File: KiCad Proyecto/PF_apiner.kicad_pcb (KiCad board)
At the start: 2 copper layers, 132 parts, among them J1 OBDII Header, J2 Conn_01x05, Q1 2N7002, Q10 2N7002, Q2 BSS314PE, Q3 BSS314PE, Q4 MMBT3904, Q5 MMBT3904, Q6 2N7002, Q7 2N7002, Q8 2N7002, Q9 BSS314PE, SW1 SW_RESET, SW2 SW_BOOT, U1 TPS54202, U10 STN2120, U11 AZ1117EH-3.3TRG1, U14 ESP32-WROOM, U2 AZ1117EH-3.3TRG1, U3 LM339, U4 MCP25612FD, U5 TH8056, U6 PESD1CAN, U7 PESD1CAN, U8 PESD1CAN, U9 LM317, Y1 16M

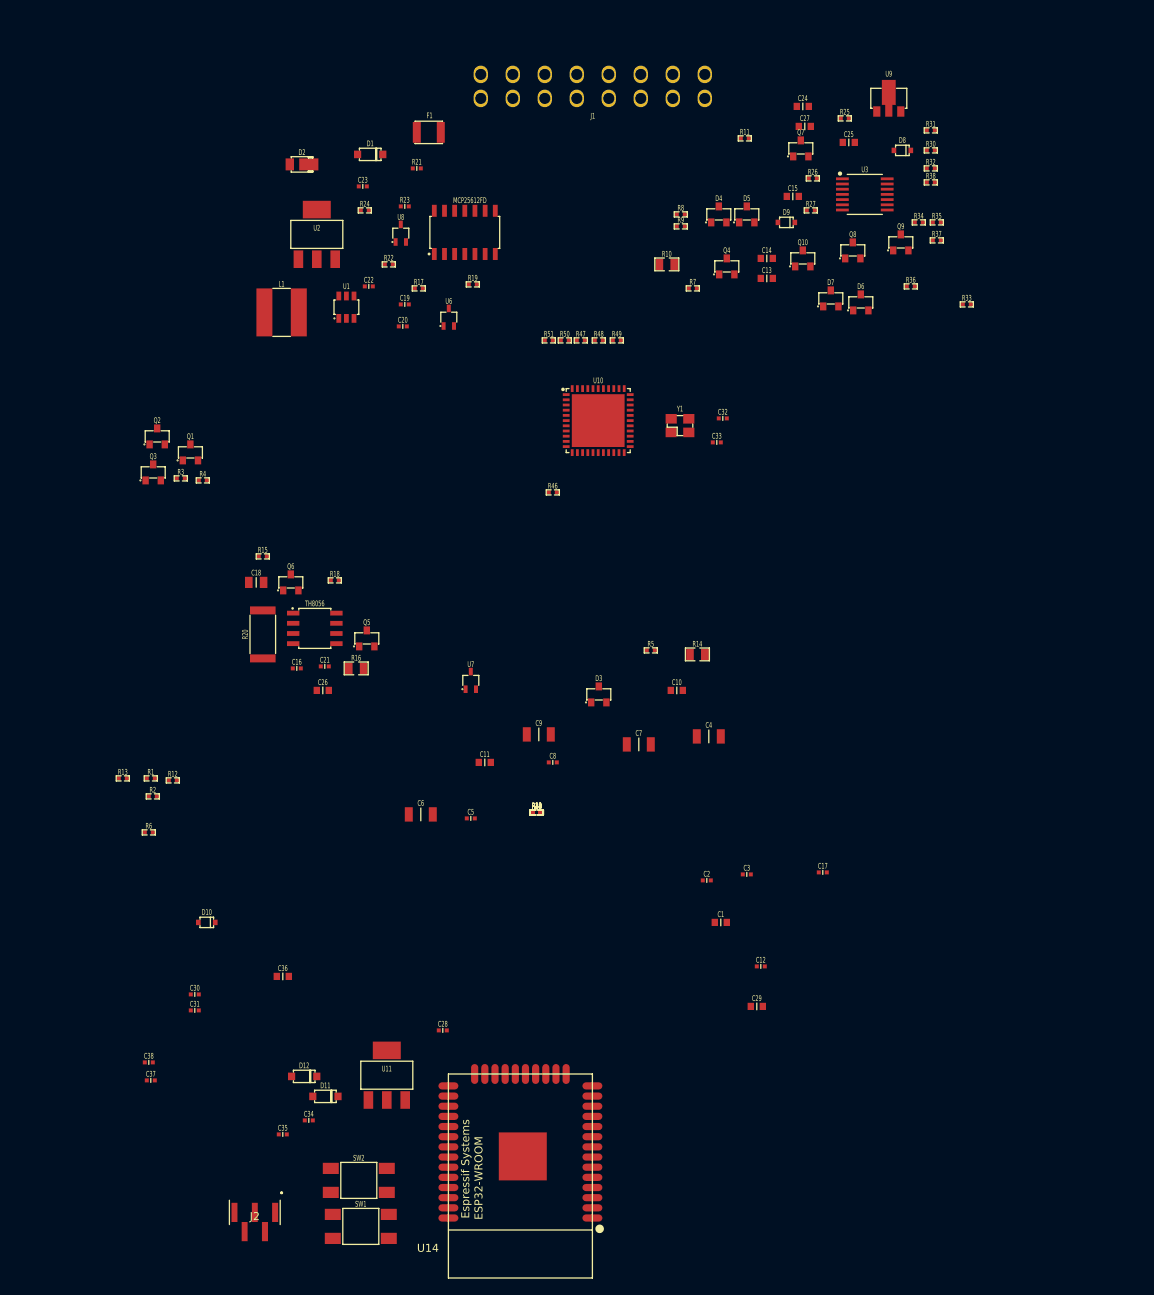
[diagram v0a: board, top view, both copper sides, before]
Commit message: added screw holes
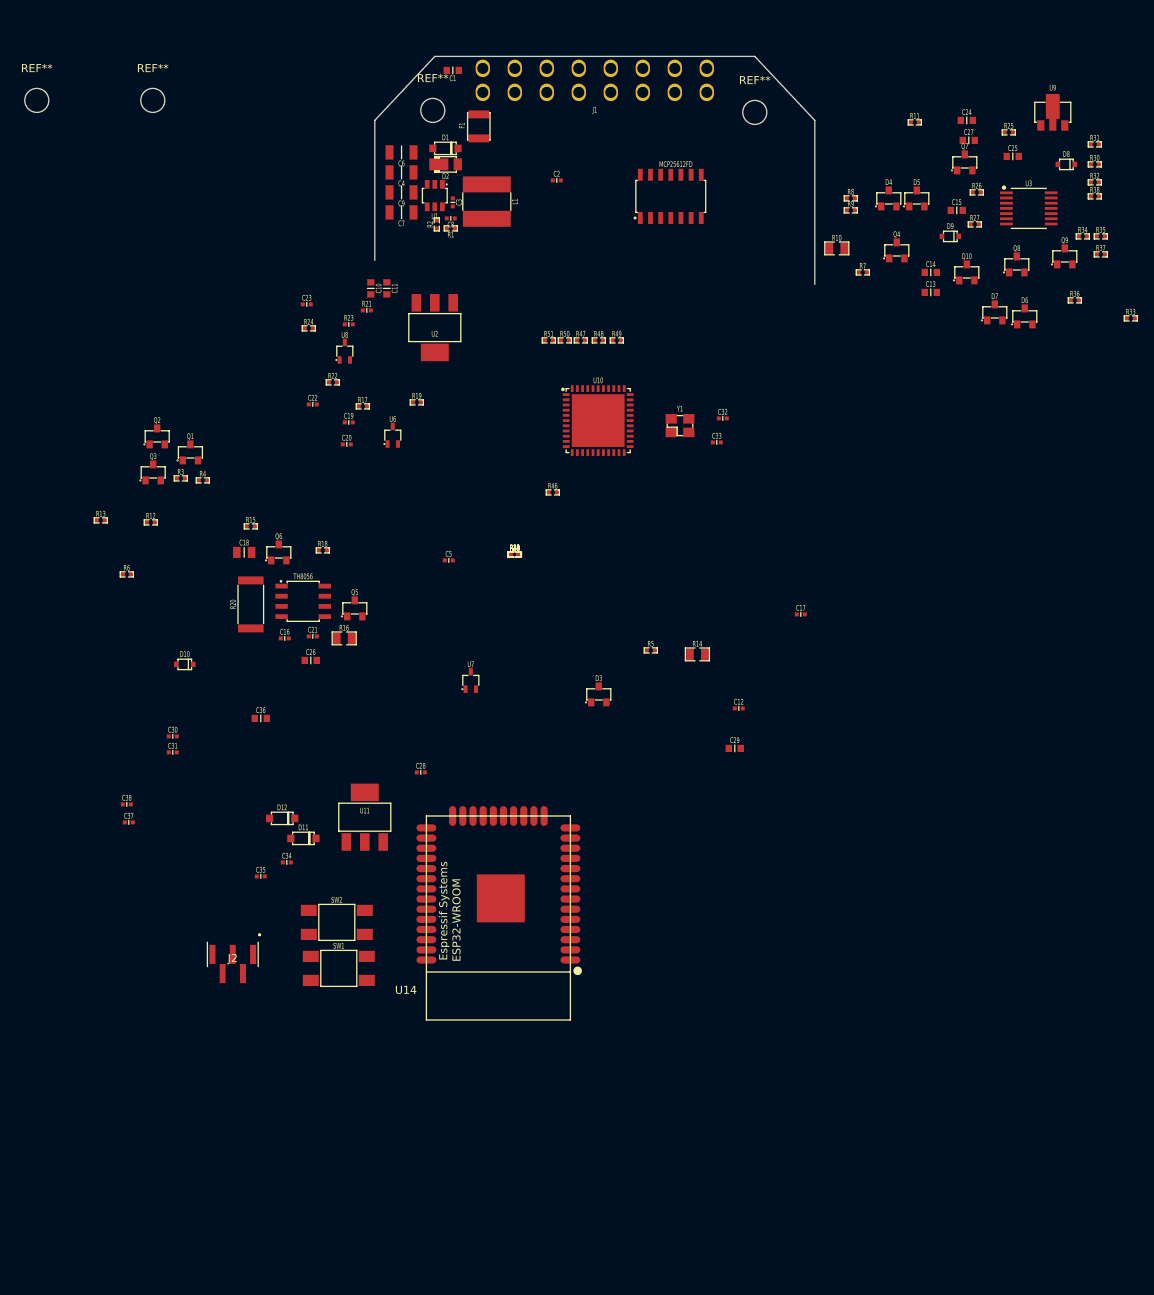
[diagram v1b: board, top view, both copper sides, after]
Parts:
- added REF**: MountingHole_3mm, misc:MountingHole_3mm, F.Cu at (125.0, 44.0)
- added REF**: MountingHole_3mm, misc:MountingHole_3mm, F.Cu at (49.8, 42.5)
- added REF**: MountingHole_3mm, misc:MountingHole_3mm, F.Cu at (35.2, 42.5)
- added REF**: MountingHole_3mm, misc:MountingHole_3mm, F.Cu at (84.8, 43.8)
- moved C1 111.6 mm to (87.2, 38.8), turned to 180 degrees
- moved C3 91.7 mm to (87.2, 55.2), turned to 270 degrees
- moved C2 89.5 mm to (100.2, 52.5)
- moved C6 82.8 mm to (80.8, 49.0), turned to 180 degrees
- moved C4 80.3 mm to (80.8, 51.5), turned to 180 degrees
- moved R2 79.8 mm to (85.2, 58.0), turned to 90 degrees
- moved R1 78.3 mm to (87.0, 58.5), turned to 180 degrees
- moved C7 72.8 mm to (80.8, 56.5), turned to 180 degrees
- moved C9 69.9 mm to (80.8, 54.0), turned to 180 degrees
- moved C8 69.2 mm to (87.0, 57.2), turned to 180 degrees
- moved C10 63.2 mm to (77.0, 66.0), turned to 270 degrees
- moved C11 60.5 mm to (79.0, 66.0), turned to 270 degrees
- moved C12 32.4 mm to (123.0, 118.5)
- moved C17 32.4 mm to (130.8, 106.8)
- moved C28 32.4 mm to (83.2, 126.5)
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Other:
- board outline added: 55 x 28.5 mm

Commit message: ME curbas PF pos pcb
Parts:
- C12, C13, C14, C15, C16, C17, C18, C19, C20, C21, C22, C23, C24, C25, C26, C27, C28, C29, C30, C31, C32, C33, D10, D3, D4, D5, D6, D7, D8, D9, Q10, Q4, Q5, Q6, Q7, Q8, Q9, R10, R11, R12, R13, R14, R15, R16, R17, R18, R19, R20, R21, R22, R23, R24, R25, R26, R27, R28, R29, R30, R31, R32, R33, R34, R35, R36, R37, R38, R39, R40, R41, R42, R43, R44, R45, R46, R47, R48, R49, R5, R50, R51, R6, R7, R8, R9, U10, U3, U4, U5, U6, U7, U8, U9, Y1: moved to B.Cu
- moved SW2 105.1 mm to (125.8, 54.5), turned to 90 degrees
- moved SW1 101.3 mm to (125.8, 64.5), turned to 90 degrees
- moved C37 98.6 mm to (122.0, 69.0), turned to 270 degrees
- moved C38 97.8 mm to (120.2, 66.2), turned to 90 degrees
- moved REF** 94.9 mm to (125.0, 73.2)
- moved C21 88.4 mm to (122.0, 38.2)
- moved R33 87.7 mm to (84.5, 63.8), turned to 270 degrees
- moved J2 86.3 mm to (93.7, 69.9), turned to 180 degrees
- moved R31 84.0 mm to (84.0, 57.5)
- moved R30 83.7 mm to (84.0, 56.5)
- moved R38 83.5 mm to (84.0, 55.5)
- moved R20 82.0 mm to (119.8, 47.2)
- moved U7 81.9 mm to (122.6, 40.1), turned to 90 degrees
- moved U14 81.5 mm to (108.7, 64.7)
- moved R16 81.3 mm to (128.0, 49.3), turned to 270 degrees
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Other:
- board size 55 x 28.5 mm -> 50 x 40.5 mm

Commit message: modificado pcb
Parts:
- removed C34: 1uF, chip_rlc:c_0402
- removed D11: MBR0520, to-sod-sot:SOD-123
- removed REF** (x4): MountingHole_3mm, misc:MountingHole_3mm
- removed U11: AZ1117EH-3.3TRG1, to-sod-sot:SOT-223
- added H1: PCB_HOLE, misc:MountingHole_3mm, F.Cu at (84.2, 73.2)
- added H2: PCB_HOLE, misc:MountingHole_3mm, F.Cu at (85.5, 43.2)
- added H3: PCB_HOLE, misc:MountingHole_3mm, F.Cu at (124.5, 43.2)
- added H4: PCB_HOLE, misc:MountingHole_3mm, F.Cu at (125.5, 72.8)
- C4, C9: moved to B.Cu
- U6, U8: moved to F.Cu
- moved R31 58.9 mm to (137.8, 33.5)
- moved R38 57.5 mm to (137.8, 35.0)
- moved SW2 43.7 mm to (83.2, 64.5), turned to 270 degrees
- moved R49 34.1 mm to (138.8, 46.2)
- moved R50 34.1 mm to (139.8, 46.2)
- moved R51 34.1 mm to (142.8, 46.2)
- moved C5 33.4 mm to (87.8, 62.8), turned to 0 degrees
- moved C27 30.6 mm to (62.5, 77.0)
- moved Q7 30.6 mm to (65.0, 73.8)
- moved R27 30.6 mm to (64.8, 76.0)
- moved Q3 28.8 mm to (71.8, 43.3)
- moved C12 28.6 mm to (135.2, 65.2)
- moved C28 28.6 mm to (138.2, 63.8)
- moved R45 28.6 mm to (137.2, 63.8)
- moved R46 28.6 mm to (140.5, 63.8)
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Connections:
- net /HS_CAN_N renamed /CAN_Transceiver/HS_CAN_LO
- net /HS_CAN_P renamed /CAN_Transceiver/HS_CAN_HI
- net /J1850_BUS+ renamed /J1850_Transceiver/J1850_BUS+
- net /J1850_BUS- renamed /J1850_Transceiver/J1850_BUS-
- net /K-LINE renamed /ISO_Transceiver/K-LINE
- net /L-LINE renamed /ISO_Transceiver/L-LINE
- net /MS_CAN_N renamed /CAN_Transceiver/MS_CAN_LO
- net /MS_CAN_P renamed /CAN_Transceiver/MS_CAN_HI
- net /SW_CAN renamed /CAN_Transceiver/SW_CAN
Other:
- copper layers 2 -> 4
- net class Default: trace_width 0.1524 -> 0.15; via_dia 0.6096 -> 0.6; via_drill 0.4064 -> 0.4
- rule trace_min: 0.1524 -> 0.15
- rule via_min_drill: 0.4064 -> 0.4
- rule via_min_size: 0.6096 -> 0.6
